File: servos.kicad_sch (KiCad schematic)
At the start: 3 parts, among them J7 90120-0763, J8 90120-0763, J9 90120-0763

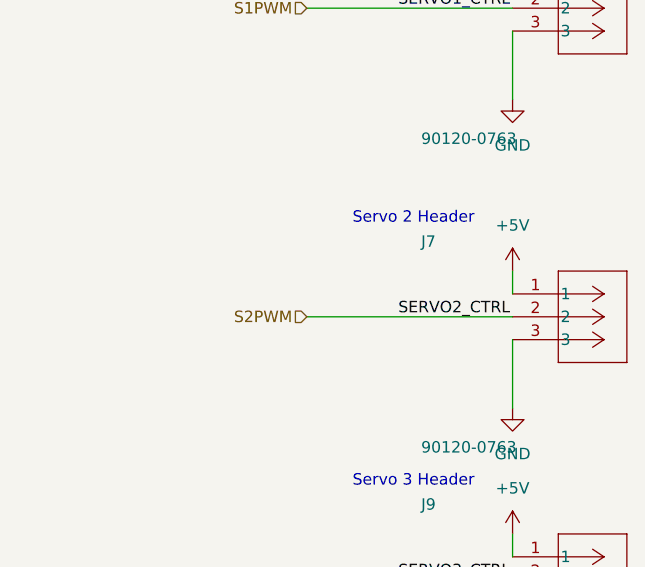
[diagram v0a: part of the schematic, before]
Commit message: Fixed Hierarchy mess
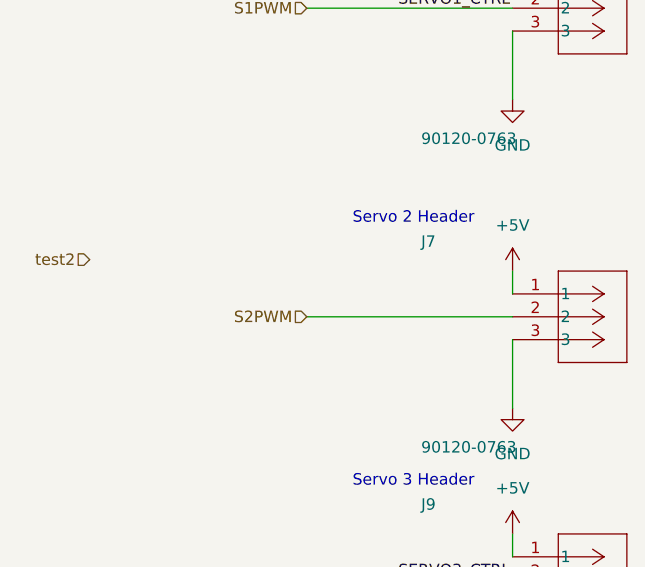
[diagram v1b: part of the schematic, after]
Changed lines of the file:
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@@
-		)
-	)
-	(label "SERVO2_CTRL"
-		(at 85.09 91.44 0)
-		(effects
-			(font
-				(size 1.27 1.27)
-			)
-			(justify left bottom)
 		)
 	)
@@
 		(effects
 			(font
+				(size 1.27 1.27)
+			)
+			(justify right)
+		)
+	)
+	(hierarchical_label "test2"
+		(shape input)
+		(at 50.8 85.09 180)
+		(effects
+			(font

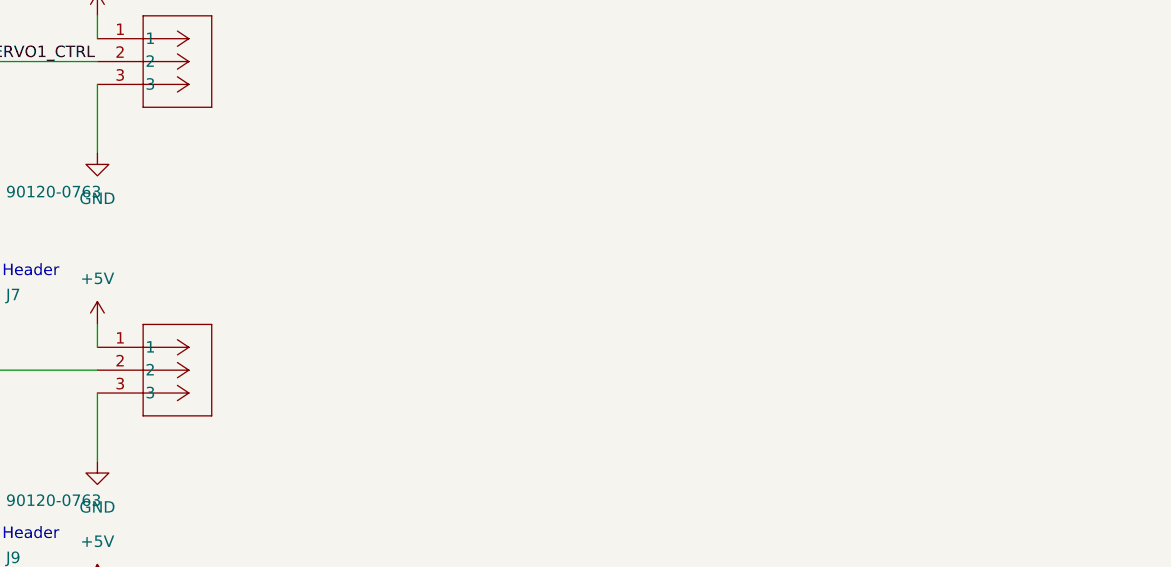
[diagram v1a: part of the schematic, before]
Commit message: clarification on servo requirements
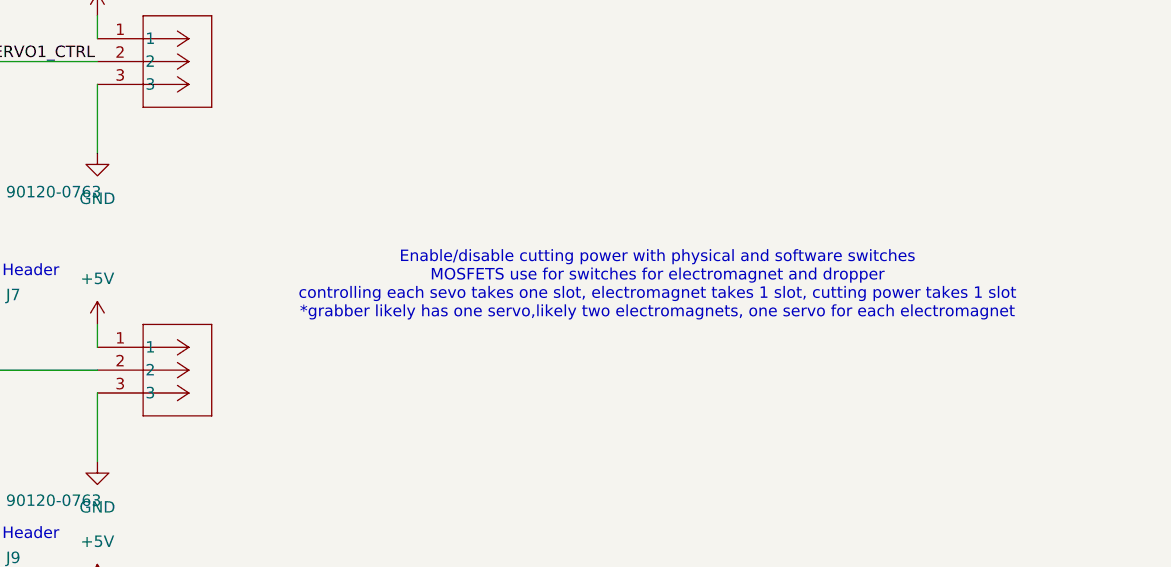
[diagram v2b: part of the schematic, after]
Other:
- note added: "Enable/disable cutting power with physical and software switches MOSFETS use for switches for electromagnet and dropper controlling each sevo takes one slot, electromagnet takes 1 slot, cutting power takes 1 slot *grabber likely has one servo,likely two electromagnets, one servo for each electromagnet"
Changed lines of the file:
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@@
+		)
+	)
+	(text "Enable/disable cutting power with physical and software switches\nMOSFETS use for switches for electromagnet and dropper\ncontrolling each sevo takes one slot, electromagnet takes 1 slot, cutting power takes 1 slot\n*grabber likely has one servo,likely two electromagnets, one servo for each electromagnet"
+		(exclude_from_sim no)
+		(at 160.02 82.042 0)
+		(effects
+			(font
+				(size 1.27 1.27)
+			)
 		)
 	)

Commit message: added footprints Servos on PCB
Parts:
- removed J7, J8, J9: 90120-0763, CONN_901200763_MOL, symbol 2024-02-03_17-19-22:901200763
- added J10, J11, J12: Conn_01x03_Pin, Connector_PinHeader_2.54mm:PinHeader_1x03_P2.54mm_Vertical, symbol Connector:Conn_01x03_Pin
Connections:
- net +5V: now also J10.3 (Pin_3), J11.3 (Pin_3), J12.3 (Pin_3)
- net GND: now also J10.1 (Pin_1), J11.1 (Pin_1), J12.1 (Pin_1)
- net S1PWM: now also J10.2 (Pin_2)
- net S2PWM: now also J12.2 (Pin_2)
- net S3PWM: now also J11.2 (Pin_2)
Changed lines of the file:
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@@
 	(wire
 		(pts
-			(xy 97.79 88.9) (xy 97.79 86.36)
+			(xy 97.79 86.36) (xy 97.79 88.9)
 		)
 		(stroke
@@
 		(stroke
 			(width 0.254)
+			(type default)
+		)
+	)
+	(wire
+		(pts
+			(xy 97.79 88.9) (xy 97.79 87.63)
+		)
+		(stroke
+			(width 0)
 			(type default)
 		)
@@
 		)
 	)
-	(hierarchical_label "test2"
-		(shape input)
-		(at 50.8 85.09 180)
-		(effects
-			(font
-				(size 1.27 1.27)
-			)
-			(justify right)
-		)
-	)
-	(symbol
-		(lib_id "2024-02-03_17-19-22:901200763")
-		(at 97.79 118.11 0)
-		(unit 1)
-		(exclude_from_sim no)
-		(in_bom yes)
-		(on_board yes)
-		(dnp no)
-		(property "Reference" "J9"
-			(at 87.63 113.03 0)
-			(effects
-				(font
-					(size 1.27 1.27)
-				)
-				(justify left bottom)
-			)
-		)
-		(property "Value" "90120-0763"
-			(at 87.63 135.89 0)
-			(effects
-				(font
-					(size 1.27 1.27)
-				)
-				(justify left bottom)
-			)
-		)
-		(property "Footprint" "CONN_901200763_MOL"
-			(at 97.79 118.11 0)
-			(effects
-				(font
-					(size 1.27 1.27)
-					(italic yes)
-				)
-				(hide yes)
-			)
-		)
-		(property "Datasheet" "901200763"
-			(at 97.79 118.11 0)
-			(effects
-				(font
-					(size 1.27 1.27)
-					(italic yes)
-				)
-				(hide yes)
-			)
-		)
-		(property "Description" ""
-			(at 97.79 118.11 0)
-			(effects
-				(font
-					(size 1.27 1.27)
-				)
-			)
-		)
-		(property "Part Number" "90120-0763"
-			(at 97.79 118.11 0)
-			(effects
-				(font
-					(size 1.27 1.27)
-				)
-				(hide yes)
-			)
-		)
-		(pin "1"
+	(symbol
+		(lib_id "Connector:Conn_01x03_Pin")
+		(at 102.87 120.65 180)
+		(unit 1)
+		(exclude_from_sim no)
+		(in_bom yes)
+		(on_board yes)
+		(dnp no)
+		(fields_autoplaced yes)
+		(property "Reference" "J11"
+			(at 104.14 119.3799 0)
+			(effects
+				(font
+					(size 1.27 1.27)
+				)
+				(justify right)
+			)
+		)
+		(property "Value" "Conn_01x03_Pin"
+			(at 104.14 121.9199 0)
+			(effects
+				(font
+					(size 1.27 1.27)
+				)
+				(justify right)
+			)
+		)
+		(property "Footprint" "Connector_PinHeader_2.54mm:PinHeader_1x03_P2.54mm_Vertical"
+			(at 102.87 120.65 0)
+			(effects
+				(font
+					(size 1.27 1.27)
+				)
+				(hide yes)
+			)
+		)
+		(property "Datasheet" "~"
+			(at 102.87 120.65 0)
+			(effects
+				(font
+					(size 1.27 1.27)
+				)
+				(hide yes)
+			)
+		)
+		(property "Description" "Generic connector, single row, 01x03, script generated"
+			(at 102.87 120.65 0)
+			(effects
+				(font
+					(size 1.27 1.27)
+				)
+				(hide yes)
+			)
+		)
+		(pin "1"
+		)
+		(pin "3"
 		)
 		(pin "2"
 		)
-		(pin "3"
-		)
 		(instances
 			(project "Expansion_dual_header"
 				(path "/45910b0a-2ab6-4912-b705-1582171f57d5/5f2248db-3d7b-40c1-9259-f6fc27549d5d"
-					(reference "J9")
+					(reference "J11")
 					(unit 1)
 				)
@@
 	)
 	(symbol
-		(lib_id "2024-02-03_17-19-22:901200763")
-		(at 97.79 88.9 0)
-		(unit 1)
-		(exclude_from_sim no)
-		(in_bom yes)
-		(on_board yes)
-		(dnp no)
-		(property "Reference" "J7"
-			(at 87.63 83.82 0)
-			(effects
-				(font
-					(size 1.27 1.27)
-				)
-				(justify left bottom)
-			)
-		)
-		(property "Value" "90120-0763"
-			(at 87.63 106.68 0)
-			(effects
-				(font
-					(size 1.27 1.27)
-				)
-				(justify left bottom)
-			)
-		)
-		(property "Footprint" "CONN_901200763_MOL"
-			(at 97.79 88.9 0)
-			(effects
-				(font
-					(size 1.27 1.27)
-					(italic yes)
-				)
-				(hide yes)
-			)
-		)
-		(property "Datasheet" "901200763"
-			(at 97.79 88.9 0)
-			(effects
-				(font
-					(size 1.27 1.27)
-					(italic yes)
-				)
-				(hide yes)
-			)
-		)
-		(property "Description" ""
-			(at 97.79 88.9 0)
-			(effects
-				(font
-					(size 1.27 1.27)
-				)
-			)
-		)
-		(property "Part Number" "90120-0763"
-			(at 97.79 88.9 0)
-			(effects
-				(font
-					(size 1.27 1.27)
-				)
-				(hide yes)
-			)
-		)
-		(pin "1"
-		)
-		(pin "2"
-		)
-		(pin "3"
-		)
-		(instances
-			(project "Expansion_dual_header"
-				(path "/45910b0a-2ab6-4912-b705-1582171f57d5/5f2248db-3d7b-40c1-9259-f6fc27549d5d"
-					(reference "J7")
-					(unit 1)
-				)
-			)
-		)
-	)
-	(symbol
 		(lib_id "power:GND")
 		(at 97.79 67.31 0)
@@
 	)
 	(symbol
-		(lib_id "2024-02-03_17-19-22:901200763")
-		(at 97.79 54.61 0)
-		(unit 1)
-		(exclude_from_sim no)
-		(in_bom yes)
-		(on_board yes)
-		(dnp no)
-		(property "Reference" "J8"
-			(at 87.63 49.53 0)
-			(effects
-				(font
-					(size 1.27 1.27)
-				)
-				(justify left bottom)
-			)
-		)
-		(property "Value" "90120-0763"
-			(at 87.63 72.39 0)
-			(effects
-				(font
-					(size 1.27 1.27)
-				)
-				(justify left bottom)
-			)
-		)
-		(property "Footprint" "CONN_901200763_MOL"
-			(at 97.79 54.61 0)
-			(effects
-				(font
-					(size 1.27 1.27)
-					(italic yes)
-				)
-				(hide yes)
-			)
-		)
-		(property "Datasheet" "901200763"
-			(at 97.79 54.61 0)
-			(effects
-				(font
-					(size 1.27 1.27)
-					(italic yes)
-				)
-				(hide yes)
-			)
-		)
-		(property "Description" ""
-			(at 97.79 54.61 0)
-			(effects
-				(font
-					(size 1.27 1.27)
-				)
-			)
-		)
-		(property "Part Number" "90120-0763"
-			(at 97.79 54.61 0)
-			(effects
-				(font
-					(size 1.27 1.27)
-				)
-				(hide yes)
-			)
-		)
-		(pin "1"
+		(lib_id "Connector:Conn_01x03_Pin")
+		(at 102.87 57.15 180)
+		(unit 1)
+		(exclude_from_sim no)
+		(in_bom yes)
+		(on_board yes)
+		(dnp no)
+		(fields_autoplaced yes)
+		(property "Reference" "J10"
+			(at 104.14 55.8799 0)
+			(effects
+				(font
+					(size 1.27 1.27)
+				)
+				(justify right)
+			)
+		)
+		(property "Value" "Conn_01x03_Pin"
+			(at 104.14 58.4199 0)
+			(effects
+				(font
+					(size 1.27 1.27)
+				)
+				(justify right)
+			)
+		)
+		(property "Footprint" "Connector_PinHeader_2.54mm:PinHeader_1x03_P2.54mm_Vertical"
+			(at 102.87 57.15 0)
+			(effects
+				(font
+					(size 1.27 1.27)
+				)
+				(hide yes)
+			)
+		)
+		(property "Datasheet" "~"
+			(at 102.87 57.15 0)
+			(effects
+				(font
+					(size 1.27 1.27)
+				)
+				(hide yes)
+			)
+		)
+		(property "Description" "Generic connector, single row, 01x03, script generated"
+			(at 102.87 57.15 0)
+			(effects
+				(font
+					(size 1.27 1.27)
+				)
+				(hide yes)
+			)
+		)
+		(pin "1"
+		)
+		(pin "3"
 		)
 		(pin "2"
 		)
+		(instances
+			(project ""
+				(path "/45910b0a-2ab6-4912-b705-1582171f57d5/5f2248db-3d7b-40c1-9259-f6fc27549d5d"
+					(reference "J10")
+					(unit 1)
+				)
+			)
+		)
+	)
+	(symbol
+		(lib_id "Connector:Conn_01x03_Pin")
+		(at 102.87 91.44 180)
+		(unit 1)
+		(exclude_from_sim no)
+		(in_bom yes)
+		(on_board yes)
+		(dnp no)
+		(fields_autoplaced yes)
+		(property "Reference" "J12"
+			(at 104.14 90.1699 0)
+			(effects
+				(font
+					(size 1.27 1.27)
+				)
+				(justify right)
+			)
+		)
+		(property "Value" "Conn_01x03_Pin"
+			(at 104.14 92.7099 0)
+			(effects
+				(font
+					(size 1.27 1.27)
+				)
+				(justify right)
+			)
+		)
+		(property "Footprint" "Connector_PinHeader_2.54mm:PinHeader_1x03_P2.54mm_Vertical"
+			(at 102.87 91.44 0)
+			(effects
+				(font
+					(size 1.27 1.27)
+				)
+				(hide yes)
+			)
+		)
+		(property "Datasheet" "~"
+			(at 102.87 91.44 0)
+			(effects
+				(font
+					(size 1.27 1.27)
+				)
+				(hide yes)
+			)
+		)
+		(property "Description" "Generic connector, single row, 01x03, script generated"
+			(at 102.87 91.44 0)
+			(effects
+				(font
+					(size 1.27 1.27)
+				)
+				(hide yes)
+			)
+		)
+		(pin "1"
+		)
 		(pin "3"
 		)
+		(pin "2"
+		)
 		(instances
 			(project "Expansion_dual_header"
 				(path "/45910b0a-2ab6-4912-b705-1582171f57d5/5f2248db-3d7b-40c1-9259-f6fc27549d5d"
-					(reference "J8")
-					(unit 1)
-				)
+					(reference "J12")
+					(unit 1)
+				)

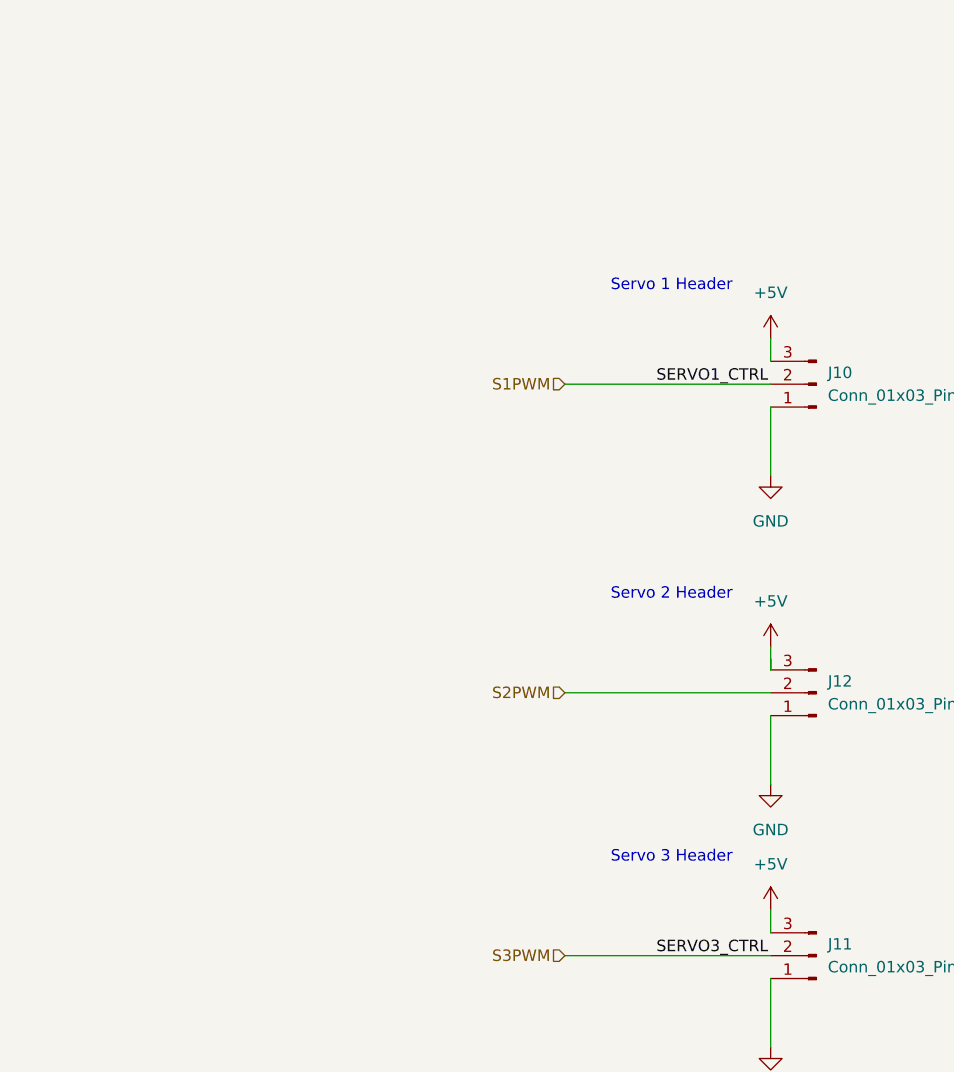
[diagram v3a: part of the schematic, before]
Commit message: added MOSFET, and switch for Servos
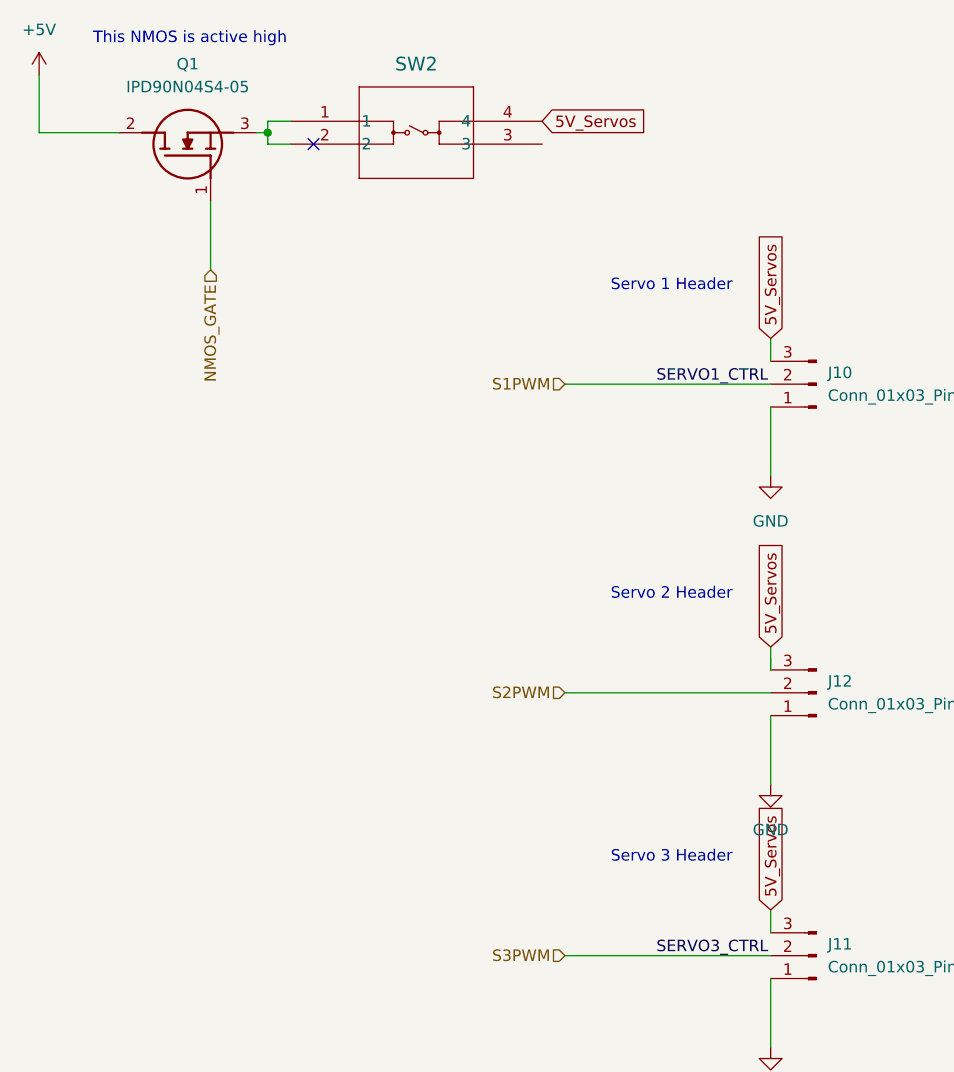
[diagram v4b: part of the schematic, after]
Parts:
- added Q1: IPD90N04S4-05, IPD90N04S405, symbol AquaPartsLib:IPD90N04S4-05
- added SW2: PTS 647 SN50 SMTR2 LFS, AquaPartsLib:SW_PTS_647_SN50_SMTR2_LFS, symbol AquaPartsLib:PTS_647_SN50_SMTR2_LFS
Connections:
- net +5V: now also Q1.2 (D); no longer J10.3 (Pin_3), J11.3 (Pin_3), J12.3 (Pin_3)
- new net: Q1.3 (S), SW2.1, SW2.2
- new net 5V_Servos: J10.3 (Pin_3), J11.3 (Pin_3), J12.3 (Pin_3), SW2.4
- new net NMOS_GATE: Q1.1 (G)
- no-connect marks 0 -> 1
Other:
- note added: "This NMOS is active high"
